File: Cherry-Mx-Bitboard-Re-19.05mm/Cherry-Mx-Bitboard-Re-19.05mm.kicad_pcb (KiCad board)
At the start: 2 copper layers, 17.8 x 17.8 mm, 21 parts, among them SW1 SW_Push, SW2 SW_Push-Switch

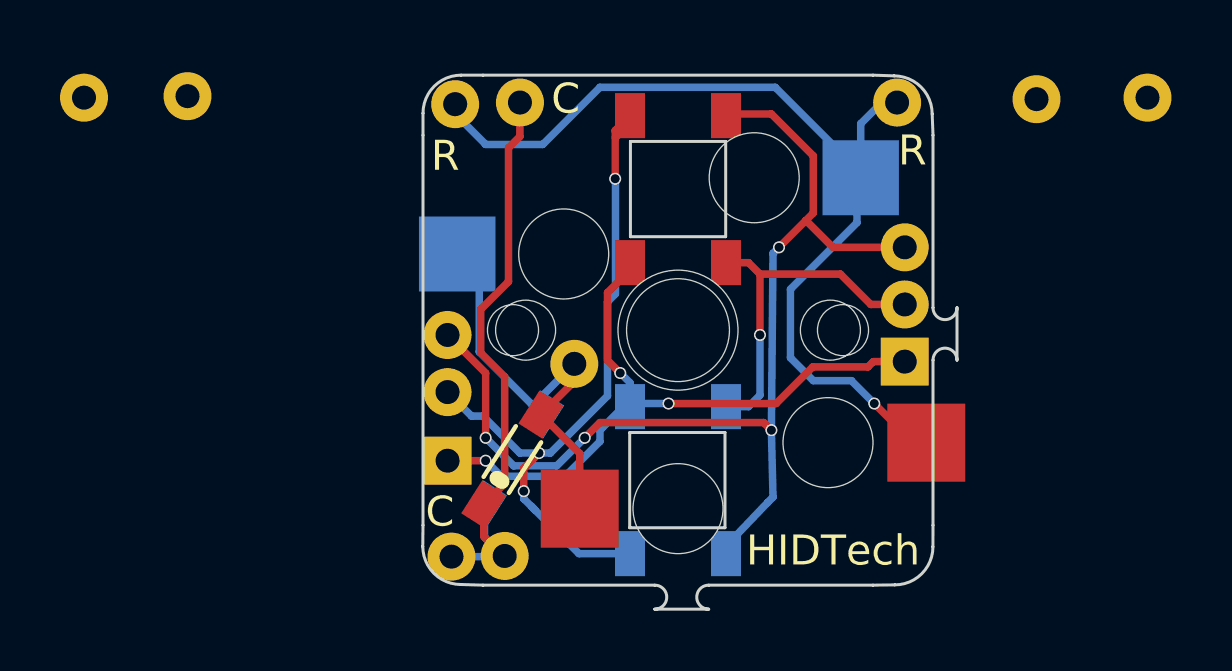
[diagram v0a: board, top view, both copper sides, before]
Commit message: flip leds so they face the right side
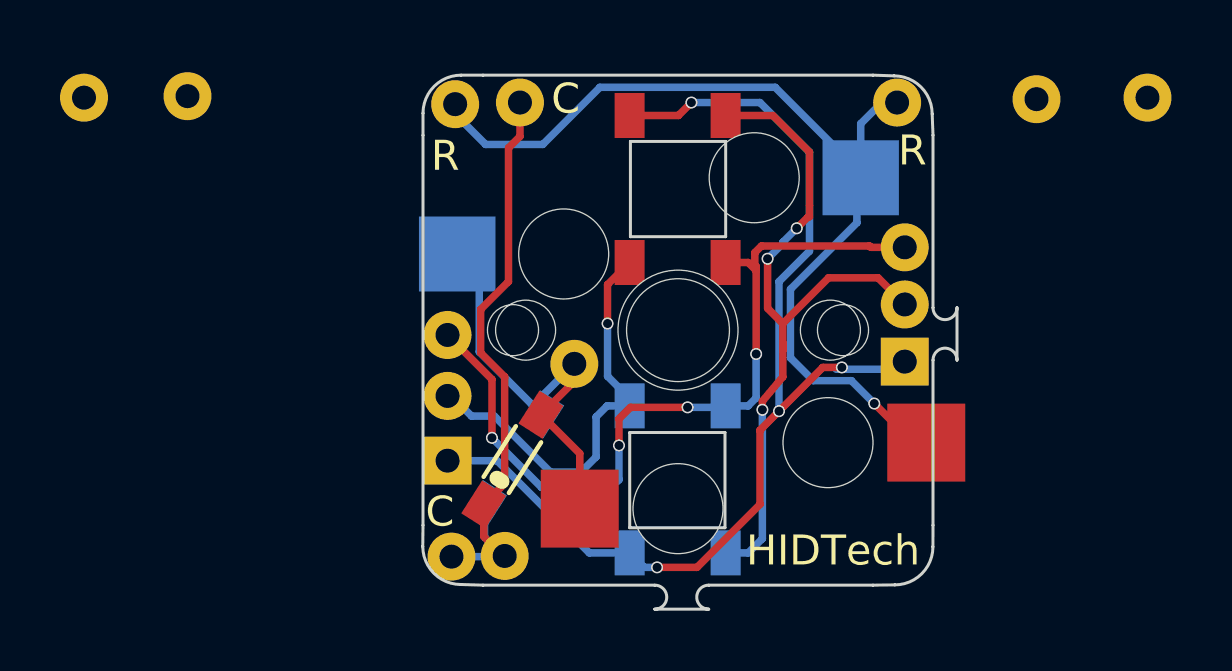
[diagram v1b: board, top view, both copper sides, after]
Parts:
- D5, D6: footprint LED_SMD:LED_SK6812_PLCC4_5.0x5.0mm_P3.2mm -> customs:LED_SK6812_PLCC4_5.0x5.0mm_P3.2mm_FLIP
- moved Dout1 0.13 mm to (85.0, 56.0)
- turned D5 to 270 degrees
- turned D6 to 90 degrees
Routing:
- net GND: track 24.6 -> 37.9 mm, vias 3 -> 4
- net Din: track 11.9 -> 24.0 mm, vias 1 -> 3
- net Dout: track 25.1 -> 14.5 mm, vias 3 -> 1
- net VCC: track 36.6 -> 27.3 mm

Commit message: Cleaned up
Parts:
- removed Col111, Col114, Row112, Row114: Conn_01x01, Footprints:Wirepad
- moved GND1 0.95 mm to (85.0, 57.2)
- moved Dout1 0.59 mm to (85.0, 55.4)
- moved Vcc1 0.53 mm to (100.3, 51.6)
- moved Din1 0.43 mm to (100.3, 53.4)
- moved Vcc2 0.36 mm to (85.0, 53.6)
- moved Col112 0.35 mm to (87.0, 46.1)
- moved GND2 0.33 mm to (100.3, 55.2)
- moved Row111 0.30 mm to (100.2, 46.2)
- moved Col113 0.25 mm to (87.0, 61.5)
- moved Row113 0.18 mm to (85.0, 46.4)
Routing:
- net Row1: track 33.6 -> 34.8 mm
- net GND: track 37.9 -> 38.8 mm, vias 4 -> 3
- net VCC: track 27.3 -> 28.0 mm, vias 4 -> 5
- net Din: track 24.0 -> 23.3 mm, vias 3 -> 1
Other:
- board size 17.8 x 17.8 mm -> 17 x 17 mm
- board text added: "Col"
- board text added: "HIDTech.ca"
- board text added: "Row"
- board text removed: "C"
- board text removed: "HIDTech"
- board text removed: "R"

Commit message: Silk
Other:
- board text added: "-"
- board text added: "<name>"
- board text added: "Choc"
- board text added: "Din"
- board text added: "Dout"
- board text added: "GND"
- board text added: "HIDTech"
- board text added: "MX"
- board text added: "VCC"
- board text removed: "HIDTech.ca"
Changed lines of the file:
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@@
   (general
     (thickness 1.6)
-    (drawings 38)
+    (drawings 69)
     (tracks 159)
     (zones 0)
@@
   )
   (layers
-    (0 F.Cu signal hide)
+    (0 F.Cu signal)
     (31 B.Cu signal)
     (32 B.Adhes user hide)
@@
     (34 B.Paste user hide)
     (35 F.Paste user hide)
-    (36 B.SilkS user hide)
+    (36 B.SilkS user)
     (37 F.SilkS user)
     (38 B.Mask user hide)
@@
       (net 3 Row1))
   )
+  (gr_line (start 91.795 62.165) (end 91.795 61.015) (layer B.SilkS) (width 0.15))
+  (gr_line (start 90.245 62.165) (end 91.795 62.165) (layer B.SilkS) (width 0.15))
+  (gr_line (start 90.245 60.165) (end 90.245 62.165) (layer B.SilkS) (width 0.15))
+  (gr_line (start 90.995 60.165) (end 90.245 60.165) (layer B.SilkS) (width 0.15))
+  (gr_line (start 90.145 47.715) (end 90.945 47.715) (layer F.SilkS) (width 0.15))
+  (gr_line (start 90.145 47.465) (end 90.145 47.715) (layer F.SilkS) (width 0.15))
+  (gr_line (start 91.845 45.665) (end 91.845 47.365) (layer F.SilkS) (width 0.15))
+  (gr_line (start 90.145 45.665) (end 91.845 45.665) (layer F.SilkS) (width 0.15))
+  (gr_line (start 90.145 47.465) (end 90.145 45.665) (layer F.SilkS) (width 0.15))
+  (gr_text <name> (at 87.9924 48.515) (layer B.SilkS)
+    (effects (font (size 0.75 0.75) (thickness 0.15)) (justify mirror))
+  )
+  (gr_text <name> (at 87.9924 48.515) (layer F.SilkS)
+    (effects (font (size 0.75 0.75) (thickness 0.15)))
+  )
+  (gr_text - (at 85.845 54.365 -40) (layer B.SilkS)
+    (effects (font (size 1 1) (thickness 0.15)) (justify mirror))
+  )
+  (gr_text VCC (at 86.695 55.165) (layer B.SilkS)
+    (effects (font (size 0.5 0.5) (thickness 0.125)) (justify mirror))
+  )
+  (gr_text "Dout\n" (at 86.745 55.865) (layer B.SilkS)
+    (effects (font (size 0.5 0.5) (thickness 0.125)) (justify mirror))
+  )
+  (gr_text GND (at 86.645 56.665) (layer B.SilkS)
+    (effects (font (size 0.5 0.5) (thickness 0.125)) (justify mirror))
+  )
+  (gr_text GND (at 86.645 56.665) (layer F.SilkS)
+    (effects (font (size 0.5 0.5) (thickness 0.125)))
+  )
+  (gr_text - (at 85.845 54.365 -40) (layer F.SilkS)
+    (effects (font (size 1 1) (thickness 0.15)))
+  )
+  (gr_text "Dout\n" (at 86.745 55.865) (layer F.SilkS)
+    (effects (font (size 0.5 0.5) (thickness 0.125)))
+  )
+  (gr_text VCC (at 86.695 55.165) (layer F.SilkS)
+    (effects (font (size 0.5 0.5) (thickness 0.125)))
+  )
+  (gr_text - (at 99.645 52.815 -40) (layer B.SilkS)
+    (effects (font (size 1 1) (thickness 0.15)) (justify mirror))
+  )
+  (gr_text GND (at 98.645 55.265) (layer B.SilkS)
+    (effects (font (size 0.5 0.5) (thickness 0.125)) (justify mirror))
+  )
+  (gr_text Din (at 98.595 52.415) (layer B.SilkS)
+    (effects (font (size 0.5 0.5) (thickness 0.125)) (justify mirror))
+  )
+  (gr_text VCC (at 98.695 51.465) (layer B.SilkS)
+    (effects (font (size 0.5 0.5) (thickness 0.125)) (justify mirror))
+  )
+  (gr_text GND (at 98.645 55.265) (layer F.SilkS)
+    (effects (font (size 0.5 0.5) (thickness 0.125)))
+  )
+  (gr_text VCC (at 98.695 51.465) (layer F.SilkS)
+    (effects (font (size 0.5 0.5) (thickness 0.125)))
+  )
+  (gr_text - (at 99.645 52.815 -40) (layer F.SilkS)
+    (effects (font (size 1 1) (thickness 0.15)))
+  )
+  (gr_text Din (at 98.595 52.415) (layer F.SilkS)
+    (effects (font (size 0.5 0.5) (thickness 0.125)))
+  )
+  (gr_text MX (at 97.945 61.365) (layer B.SilkS)
+    (effects (font (size 1 1) (thickness 0.15)) (justify mirror))
+  )
+  (gr_text Choc (at 97.895 61.365) (layer F.SilkS)
+    (effects (font (size 1 1) (thickness 0.15)))
+  )
+  (gr_text "Rev 2.0\n" (at 97.8924 60.115) (layer F.SilkS)
+    (effects (font (size 0.75 0.75) (thickness 0.15)))
+  )
+  (gr_text HIDTech (at 95.695 53.515 -90) (layer B.SilkS)
+    (effects (font (size 0.75 0.75) (thickness 0.15)) (justify mirror))
+  )
   (gr_line (start 91.869998 62.314999) (end 93.67 62.315001) (layer Edge.Cuts) (width 0.1))
   (gr_line (start 101.144999 53.065) (end 101.145 54.815) (layer Edge.Cuts) (width 0.1))
@@
   (gr_line (start 86.145 45.315001) (end 85.415 45.314999) (layer Edge.Cuts) (width 0.1))
   (gr_arc (start 85.415 46.584999) (end 85.415 45.314999) (angle -90) (layer Edge.Cuts) (width 0.1))
-  (gr_text "Rev 2.0\n" (at 97.9424 61.087) (layer B.SilkS)
-    (effects (font (size 1 1) (thickness 0.15)) (justify mirror))
-  )
-  (gr_text HIDTech.ca (at 95.795 53.865 -90) (layer F.SilkS)
+  (gr_text "Rev 2.0\n" (at 97.9424 60.115) (layer B.SilkS)
+    (effects (font (size 0.75 0.75) (thickness 0.15)) (justify mirror))
+  )
+  (gr_text HIDTech (at 95.695 53.565 -90) (layer F.SilkS)
     (effects (font (size 0.75 0.75) (thickness 0.15)))
   )

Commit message: Break tabs
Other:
- board size 17 x 17 mm -> 18 x 18 mm
- board text added: "Kompacted"
- board text removed: "<name>"

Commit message: routing
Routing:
- net Row1: track 34.8 -> 12.0 mm
- net GND: track 38.8 -> 18.8 mm, vias 3 -> 6
- net VCC: track 28.0 -> 13.7 mm, vias 5 -> 4
- net Net-(D1-Pad2): track 17.6 -> 7.84 mm
- net Dout: track 14.8 -> 10.4 mm
- net Col1: track 21.2 -> 18.9 mm
- net Din: track 23.3 -> 23.1 mm, vias 1 -> 3
- added copper zone on B.Cu, net Col1
- added copper zone on F.Cu, net Col1
- added copper zone on F.Cu, net Dout
- added copper zone on B.Cu, net GND
- added copper zone on F.Cu, net GND
- added copper zone on B.Cu, net Net-(D1-Pad2)
- added copper zone on F.Cu, net Net-(D1-Pad2)
- added copper zone on B.Cu, net Row1
- added copper zone on B.Cu, net VCC
- added copper zone on F.Cu, net VCC
